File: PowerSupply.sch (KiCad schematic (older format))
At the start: 5 parts

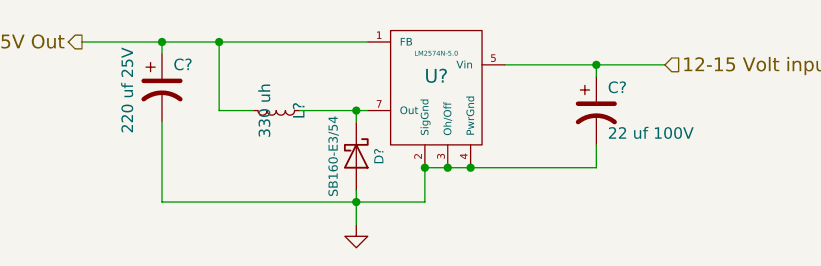
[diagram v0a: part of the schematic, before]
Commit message: Start on LCC <=> PNET router.
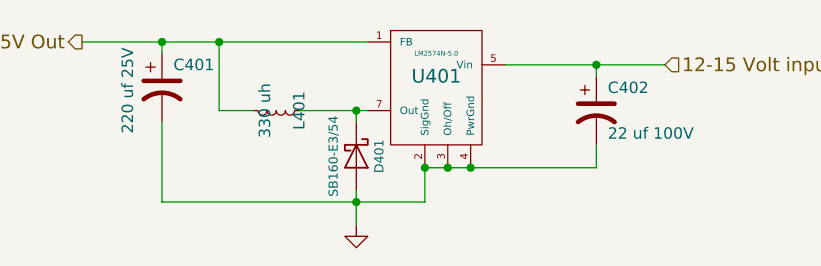
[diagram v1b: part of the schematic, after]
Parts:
- gave numbers to parts that had none: 5
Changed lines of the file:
@@
 $EndDescr
 $Comp
-L LM2574N-5.0 U?
+L LM2574N-5.0 U401
 U 1 1 63C065F7
 P 5850 3450
-F 0 "U?" H 5850 3500 60  0000 C CNN
+F 0 "U401" H 5850 3500 60  0000 C CNN
 F 1 "LM2574N-5.0" H 5850 3600 21  0000 C CNN
 F 2 "~" H 5850 3450 60  0000 C CNN
@@
 $EndComp
 $Comp
-L L_Small L?
+L L_Small L401
 U 1 1 63C065F8
 P 5150 3550
-F 0 "L?" H 5150 3650 50  0000 C CNN
+F 0 "L401" H 5150 3650 50  0000 C CNN
 F 1 "330 uh" H 5150 3500 50  0000 C CNN
 F 2 "PE-LowProfile" H 5150 3550 60  0001 C CNN
@@
 	4300 3250 5550 3250
 $Comp
-L CP1 C?
+L CP1 C401
 U 1 1 63C065F9
 P 4650 3450
-F 0 "C?" H 4700 3550 50  0000 L CNN
+F 0 "C401" H 4700 3550 50  0000 L CNN
 F 1 "220 uf 25V" V 4500 3250 50  0000 L CNN
 F 2 "C1-3V8" H 4650 3450 60  0001 C CNN
@@
 Connection ~ 4900 3250
 $Comp
-L GND #PWR?
+L GND #PWR028
 U 1 1 63C065FA
 P 5500 4050
-F 0 "#PWR?" H 5500 4050 30  0001 C CNN
+F 0 "#PWR028" H 5500 4050 30  0001 C CNN
 F 1 "GND" H 5500 3980 30  0001 C CNN
 F 2 "" H 5500 4050 60  0000 C CNN
@@
 Connection ~ 5800 3800
 $Comp
-L CP1 C?
+L CP1 C402
 U 1 1 63C065FB
 P 6550 3550
-F 0 "C?" H 6600 3650 50  0000 L CNN
+F 0 "C402" H 6600 3650 50  0000 L CNN
 F 1 "22 uf 100V" H 6600 3450 50  0000 L CNN
 F 2 "C1-3V8" H 6550 3550 60  0001 C CNN
@@
 Connection ~ 6000 3800
 $Comp
-L D_Schottky D?
+L D_Schottky D401
 U 1 1 63C065FC
 P 5500 3750
-F 0 "D?" H 5500 3850 40  0000 C CNN
+F 0 "D401" H 5500 3850 40  0000 C CNN
 F 1 "SB160-E3/54" H 5500 3650 40  0000 C CNN
 F 2 "DO-41" H 5500 3750 60  0001 C CNN
@@
 Connection ~ 5500 3550
 Wire Wire Line
-	5800 3950 5800 3800
+	5800 3800 5800 3950
 Wire Wire Line
-	4650 3950 5800 3950
+	5800 3950 4650 3950
 Wire Wire Line
 	5500 3900 5500 4050
 Wire Wire Line
-	4650 3600 4650 3950
+	4650 3950 4650 3600
 Connection ~ 5500 3950
 Text HLabel 4300 3250 0    60   Output ~ 0

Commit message: Start on PCB layout.
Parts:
- C401: footprint C1-3V8 -> Capacitors_THT:CP_Radial_D8.0mm_P3.50mm; Part Number REA221M1EBK-0811P -> 710-860080474010
- C402: footprint C1-3V8 -> Capacitors_THT:CP_Radial_D8.0mm_P3.50mm; Part Number REA220M2ABK-0811P -> 667-ECA-1VM220I
- D401: footprint DO-41 -> Diodes_THT:D_DO-41_SOD81_P7.62mm_Horizontal; Mouser Part Number (none) -> 750-SB160E-G; Part Number SB160-E3/54 -> (none)
- L401: footprint PE-LowProfile -> PELowProfile:PE-LowProfile
- U401: footprint ~ -> Housings_DIP:DIP-8_W7.62mm
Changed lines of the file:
@@
 F 0 "U401" H 5850 3500 60  0000 C CNN
 F 1 "LM2574N-5.0" H 5850 3600 21  0000 C CNN
-F 2 "~" H 5850 3450 60  0000 C CNN
+F 2 "Housings_DIP:DIP-8_W7.62mm" H 5850 3450 60  0001 C CNN
 F 3 "~" H 5850 3450 60  0000 C CNN
 	1    5850 3450
@@
 F 0 "L401" H 5150 3650 50  0000 C CNN
 F 1 "330 uh" H 5150 3500 50  0000 C CNN
-F 2 "PE-LowProfile" H 5150 3550 60  0001 C CNN
+F 2 "PELowProfile:PE-LowProfile" H 5150 3550 60  0001 C CNN
 F 3 "~" H 5150 3550 60  0000 C CNN
 F 4 "PE-52627NL" H 5150 3550 60  0001 C CNN "Part Number"
@@
 F 0 "C401" H 4700 3550 50  0000 L CNN
 F 1 "220 uf 25V" V 4500 3250 50  0000 L CNN
-F 2 "C1-3V8" H 4650 3450 60  0001 C CNN
+F 2 "Capacitors_THT:CP_Radial_D8.0mm_P3.50mm" H 4650 3450 60  0001 C CNN
 F 3 "~" H 4650 3450 60  0000 C CNN
-F 4 "REA221M1EBK-0811P" H 4650 3450 60  0001 C CNN "Part Number"
+F 4 "710-860080474010" H 4650 3450 60  0001 C CNN "Part Number"
 	1    4650 3450
 	1    0    0    -1
@@
 F 0 "C402" H 6600 3650 50  0000 L CNN
 F 1 "22 uf 100V" H 6600 3450 50  0000 L CNN
-F 2 "C1-3V8" H 6550 3550 60  0001 C CNN
+F 2 "Capacitors_THT:CP_Radial_D8.0mm_P3.50mm" H 6550 3550 60  0001 C CNN
 F 3 "~" H 6550 3550 60  0000 C CNN
-F 4 "REA220M2ABK-0811P" H 6550 3550 60  0001 C CNN "Part Number"
+F 4 "667-ECA-1VM220I" H 6550 3550 60  0001 C CNN "Part Number"
 	1    6550 3550
 	1    0    0    -1
@@
 F 0 "D401" H 5500 3850 40  0000 C CNN
 F 1 "SB160-E3/54" H 5500 3650 40  0000 C CNN
-F 2 "DO-41" H 5500 3750 60  0001 C CNN
+F 2 "Diodes_THT:D_DO-41_SOD81_P7.62mm_Horizontal" H 5500 3750 60  0001 C CNN
 F 3 "~" H 5500 3750 60  0000 C CNN
-F 4 "SB160-E3/54 " H 5500 3750 60  0001 C CNN "Part Number"
+F 4 "750-SB160E-G" H 5500 3750 60  0001 C CNN "Mouser Part Number"
 	1    5500 3750
 	0    1    1    0

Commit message: Completed initial HW design.
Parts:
- removed C401: 220 uf 25V, Capacitors_THT:CP_Radial_D8.0mm_P3.50mm, symbol CP1
- removed C402: 22 uf 100V, Capacitors_THT:CP_Radial_D8.0mm_P3.50mm, symbol CP1
- removed D401: SB160-E3/54, Diodes_THT:D_DO-41_SOD81_P7.62mm_Horizontal, symbol D_Schottky
- removed U401: LM2574N-5.0, Housings_DIP:DIP-8_W7.62mm, symbol LM2574N-5.0
- added C401: 10uf, Capacitors_SMD:CP_Elec_5x5.3, symbol CP1_Small
- added C402: 100nf, Capacitors_SMD:C_0603, symbol C_Small
- added C403, C404: 22uf, Capacitors_SMD:C_0603, symbol C_Small
- added U401: AP63205, TO_SOT_Packages_SMD:TSOT-23-6_MK06A, symbol AP63205
- L401: value 330 uh -> 4.7uH; footprint PELowProfile:PE-LowProfile -> Inductors_SMD:L_7.3x7.3_H4.5; Mouser Part Number (none) -> 81-B1047AS-4R7NP3; Part Number PE-52627NL -> (none)
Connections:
- net 12-15 Volt input: now also C401.1, U401.2 (EN), U401.3 (Vin)
- net GND: now also C401.2, C403.2, C404.2, U401.4 (GND)
- net +5V: now reaches L401.1
- net +5V: now also C403.1, C404.1, U401.1 (FB)
- net 5V Out: no longer names the net of L401.2
- net 5V Out: now also C402.2, U401.5 (SW)
- new net: C402.1, U401.6 (BST)
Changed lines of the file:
@@
 LIBS:lm2574n-5
 LIBS:sn65hvd233-ht
+LIBS:ap63205
 LIBS:LCC-PNET-Router-cache
 EELAYER 25 0
 EELAYER END
-$Descr A4 11693 8268
+$Descr USLetter 11000 8500
 encoding utf-8
 Sheet 4 4
-Title ""
-Date "4 mar 2019"
-Rev ""
-Comp ""
-Comment1 ""
+Title "ESP32 S3 Multifunction Board Universal Turnout"
+Date ""
+Rev "1.0"
+Comp "Deepwoods Software"
+Comment1 "Power Supply"
 Comment2 ""
 Comment3 ""
@@
 $EndDescr
 $Comp
-L LM2574N-5.0 U401
-U 1 1 63C065F7
-P 5850 3450
-F 0 "U401" H 5850 3500 60  0000 C CNN
-F 1 "LM2574N-5.0" H 5850 3600 21  0000 C CNN
-F 2 "Housings_DIP:DIP-8_W7.62mm" H 5850 3450 60  0001 C CNN
-F 3 "~" H 5850 3450 60  0000 C CNN
-	1    5850 3450
+L +5V #PWR402
+U 1 1 6411E143
+P 5600 4700
+F 0 "#PWR402" H 5600 4550 50  0001 C CNN
+F 1 "+5V" H 5600 4840 50  0000 C CNN
+F 2 "" H 5600 4700 50  0001 C CNN
+F 3 "" H 5600 4700 50  0001 C CNN
+	1    5600 4700
+	1    0    0    -1
+$EndComp
+$Comp
+L AP63205 U401
+U 1 1 6411E144
+P 4275 4775
+F 0 "U401" H 4275 4775 60  0000 C CNN
+F 1 "AP63205" H 4275 4875 60  0000 C CNN
+F 2 "TO_SOT_Packages_SMD:TSOT-23-6_MK06A" H 4275 4775 60  0001 C CNN
+F 3 "" H 4275 4775 60  0001 C CNN
+F 4 "621-AP63205WU-7" H 4275 4775 60  0001 C CNN "Mouser Part Number"
+	1    4275 4775
+	1    0    0    -1
+$EndComp
+$Comp
+L CP1_Small C401
+U 1 1 6411E145
+P 3600 4800
+F 0 "C401" H 3610 4870 50  0000 L CNN
+F 1 "10uf" H 3610 4720 50  0000 L CNN
+F 2 "Capacitors_SMD:CP_Elec_5x5.3" H 3600 4800 50  0001 C CNN
+F 3 "" H 3600 4800 50  0001 C CNN
+F 4 "710-865230542002" H 3600 4800 60  0001 C CNN "Mouser Part Number"
+	1    3600 4800
+	1    0    0    -1
+$EndComp
+$Comp
+L GND #PWR401
+U 1 1 6411E146
+P 3600 5075
+F 0 "#PWR401" H 3600 4825 50  0001 C CNN
+F 1 "GND" H 3600 4925 50  0000 C CNN
+F 2 "" H 3600 5075 50  0001 C CNN
+F 3 "" H 3600 5075 50  0001 C CNN
+	1    3600 5075
+	1    0    0    -1
+$EndComp
+$Comp
+L C_Small C402
+U 1 1 6411E147
+P 4900 4675
+F 0 "C402" H 4910 4745 50  0000 L CNN
+F 1 "100nf" H 4910 4595 50  0000 L CNN
+F 2 "Capacitors_SMD:C_0603" H 4900 4675 50  0001 C CNN
+F 3 "" H 4900 4675 50  0001 C CNN
+F 4 "710-885012206020" H 4900 4675 60  0001 C CNN "Mouser Part Number"
+	1    4900 4675
 	1    0    0    -1
 $EndComp
 $Comp
 L L_Small L401
-U 1 1 63C065F8
-P 5150 3550
-F 0 "L401" H 5150 3650 50  0000 C CNN
-F 1 "330 uh" H 5150 3500 50  0000 C CNN
-F 2 "PELowProfile:PE-LowProfile" H 5150 3550 60  0001 C CNN
-F 3 "~" H 5150 3550 60  0000 C CNN
-F 4 "PE-52627NL" H 5150 3550 60  0001 C CNN "Part Number"
-	1    5150 3550
+U 1 1 6411E148
+P 5175 4775
+F 0 "L401" H 5205 4815 50  0000 L CNN
+F 1 "4.7uH" H 5205 4735 50  0000 L CNN
+F 2 "Inductors_SMD:L_7.3x7.3_H4.5" H 5175 4775 50  0001 C CNN
+F 3 "" H 5175 4775 50  0001 C CNN
+F 4 "81-B1047AS-4R7NP3" H 5175 4775 60  0001 C CNN "Mouser Part Number"
+	1    5175 4775
 	0    1    1    0
 $EndComp
-Wire Wire Line
-	4900 3550 4900 3250
-Wire Wire Line
-	4300 3250 5550 3250
 $Comp
-L CP1 C401
-U 1 1 63C065F9
-P 4650 3450
-F 0 "C401" H 4700 3550 50  0000 L CNN
-F 1 "220 uf 25V" V 4500 3250 50  0000 L CNN
-F 2 "Capacitors_THT:CP_Radial_D8.0mm_P3.50mm" H 4650 3450 60  0001 C CNN
-F 3 "~" H 4650 3450 60  0000 C CNN
-F 4 "710-860080474010" H 4650 3450 60  0001 C CNN "Part Number"
-	1    4650 3450
-	1    0    0    -1
-$EndComp
-Connection ~ 4900 3250
-$Comp
-L GND #PWR028
-U 1 1 63C065FA
-P 5500 4050
-F 0 "#PWR028" H 5500 4050 30  0001 C CNN
-F 1 "GND" H 5500 3980 30  0001 C CNN
-F 2 "" H 5500 4050 60  0000 C CNN
-F 3 "" H 5500 4050 60  0000 C CNN
-	1    5500 4050
+L C_Small C403
+U 1 1 6411E149
+P 5375 4875
+F 0 "C403" H 5385 4945 50  0000 L CNN
+F 1 "22uf" H 5385 4795 50  0000 L CNN
+F 2 "Capacitors_SMD:C_0603" H 5375 4875 50  0001 C CNN
+F 3 "" H 5375 4875 50  0001 C CNN
+F 4 "603-CC0603MRX6S5B226" H 5375 4875 60  0001 C CNN "Mouser Part Number"
+	1    5375 4875
 	1    0    0    -1
 $EndComp
 Wire Wire Line
-	6550 3800 5800 3800
-Connection ~ 5900 3800
-Connection ~ 5800 3800
+	3350 4600 3850 4600
+Wire Wire Line
+	3850 4600 3850 4775
+Wire Wire Line
+	3600 4700 3600 4600
+Connection ~ 3600 4600
+Wire Wire Line
+	3600 4900 3600 5075
+Wire Wire Line
+	4775 4550 4775 4600
+Wire Wire Line
+	4775 4550 4900 4550
+Wire Wire Line
+	4900 4550 4900 4575
+Wire Wire Line
+	4775 4775 5075 4775
+Connection ~ 4900 4775
+Wire Wire Line
+	5275 4775 5600 4775
 $Comp
-L CP1 C402
-U 1 1 63C065FB
-P 6550 3550
-F 0 "C402" H 6600 3650 50  0000 L CNN
-F 1 "22 uf 100V" H 6600 3450 50  0000 L CNN
-F 2 "Capacitors_THT:CP_Radial_D8.0mm_P3.50mm" H 6550 3550 60  0001 C CNN
-F 3 "~" H 6550 3550 60  0000 C CNN
-F 4 "667-ECA-1VM220I" H 6550 3550 60  0001 C CNN "Part Number"
-	1    6550 3550
+L C_Small C404
+U 1 1 6411E14A
+P 5600 4875
+F 0 "C404" H 5610 4945 50  0000 L CNN
+F 1 "22uf" H 5610 4795 50  0000 L CNN
+F 2 "Capacitors_SMD:C_0603" H 5600 4875 50  0001 C CNN
+F 3 "" H 5600 4875 50  0001 C CNN
+F 4 "603-CC0603MRX6S5B226" H 5600 4875 60  0001 C CNN "Mouser Part Number"
+	1    5600 4875
 	1    0    0    -1
 $EndComp
+Connection ~ 5375 4775
 Wire Wire Line
-	6150 3350 6850 3350
+	5600 4775 5600 4700
 Wire Wire Line
-	6550 3700 6550 3800
-Connection ~ 6000 3800
-$Comp
-L D_Schottky D401
-U 1 1 63C065FC
-P 5500 3750
-F 0 "D401" H 5500 3850 40  0000 C CNN
-F 1 "SB160-E3/54" H 5500 3650 40  0000 C CNN
-F 2 "Diodes_THT:D_DO-41_SOD81_P7.62mm_Horizontal" H 5500 3750 60  0001 C CNN
-F 3 "~" H 5500 3750 60  0000 C CNN
-F 4 "750-SB160E-G" H 5500 3750 60  0001 C CNN "Mouser Part Number"
-	1    5500 3750
-	0    1    1    0
-$EndComp
+	3875 5225 5375 5225
 Wire Wire Line
-	5250 3550 5550 3550
-Connection ~ 5500 3550
+	3875 5225 3875 5000
 Wire Wire Line
-	5800 3800 5800 3950
+	3875 5000 3600 5000
+Connection ~ 3600 5000
 Wire Wire Line
-	5800 3950 4650 3950
+	5275 4950 4775 4950
 Wire Wire Line
-	5500 3900 5500 4050
+	5275 4950 5275 4775
 Wire Wire Line
-	4650 3950 4650 3600
-Connection ~ 5500 3950
-Text HLabel 4300 3250 0    60   Output ~ 0
-5V Out
-Connection ~ 4650 3250
-Text HLabel 6850 3350 2    60   Input ~ 0
+	5600 4975 5375 4975
+Wire Wire Line
+	5375 4975 5375 5225
+Connection ~ 4275 5225
+Text HLabel 3350 4600 0    60   Input ~ 0
 12-15 Volt input
-Connection ~ 6550 3350
-Wire Wire Line
-	4650 3300 4650 3250
-Wire Wire Line
-	4900 3550 5050 3550
-Wire Wire Line
-	5500 3600 5500 3550
-Wire Wire Line
-	6550 3400 6550 3350
 $EndSCHEMATC
